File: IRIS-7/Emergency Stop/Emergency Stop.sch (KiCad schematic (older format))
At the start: 0 parts

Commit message: Setup the 12V buck converter
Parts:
- added C?: 100nF, symbol C_Small
- added C?: 2.2uF, symbol C
- added C?: 4.7uF, symbol C
- added D?: MBRS1100T3G, symbol D_Schottky
- added IC?: LMR16006X, symbol LMR16006X
- added JP1: JP_NC, symbol JP_NC
- added L?: 220uH, symbol L
- added P?: CONN_01X02, symbol CONN_01X02
- added P?: ESTOP, symbol SPST
- added R?: 88.7k, symbol R_Small
- added R?: 6.04k, symbol R_Small
- added R?: 620k, symbol R_Small
- added R?: 20k, symbol R_Small
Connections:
- net labels added: +12V, BOOT, FB, GND, SW
- wire segments 0 -> 36
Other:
- note added: "JP1—UVLO\nOpen: Disabled\nShort: Enabled"
- note added: "TODO:\n- Verify switch voltage rating"
- note added: "UVLO occurs at 40Vin"

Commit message: Add startup control to schematic
Schematic is now ready for layout
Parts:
- added C4: 4.7uF, symbol C
- added C5, C6: 1uF, Capacitors_SMD:C_0805, symbol C_Small
- added D2: Blue, LEDs:LED_0805, symbol Led_Small
- added D3: Green, LEDs:LED_0805, symbol Led_Small
- added D4: SMAJ40CA, Diodes_SMD:D_SMA_Standard, symbol TVS
- added J1: Pwr, Terminal_Blocks:TerminalBlock_Pheonix_MPT-2.54mm_4pol, symbol SPST-NOmC-LED
- added J2: Contactor, Terminal_Blocks:TerminalBlock_Pheonix_MKDS1.5-2pol, symbol CONN_01X02
- added JP2: JP_NO, Socket_Strips:Socket_Strip_Straight_1x02_Pitch2.54mm, symbol JP_NO
- added Q1, Q2: BSS123, TO_SOT_Packages_SMD:SOT-23, symbol BSS123
- added Q3: DMP3099L, TO_SOT_Packages_SMD:SOT-23, symbol DMP3099L
- added R10, R11, R5, R6, R7, R9: 10k, Resistors_SMD:R_0805, symbol R_Small
- added R8: 100k, Resistors_SMD:R_0805, symbol R_Small
- IC1: renamed from IC?; value LMR16006X -> LMR16006; symbol LMR16006X -> LMR16006
- JP1: footprint (none) -> Socket_Strips:Socket_Strip_Straight_1x02_Pitch2.54mm
- R1, R2, R3, R4: renamed from R?; footprint (none) -> Resistors_SMD:R_0805
- gave numbers to parts that had none: 7
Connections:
- net labels added: 12Vout, EN, ~EN
- wire segments 36 -> 69
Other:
- note added: "12V DC-DC Converter"
- note added: "Emergency Stop Control Logic"
- note added: "Enables IRIS-7 when the Estop is closed\nand the power button has been pressed"
- note added: "JP2—Startup Control\nOpen: Button press required\nShort: Immediate startup"
- note added: "Powers the main relay when the\nestop button is not pressed and\nthe input voltage is above 40V"
- note added: "τ = 100ms"
- note added: "τ = 10ms"
- moved on the sheet: C1, C2, C3, D1, JP1, L1, P1, P2, R1, R2, R3, R4

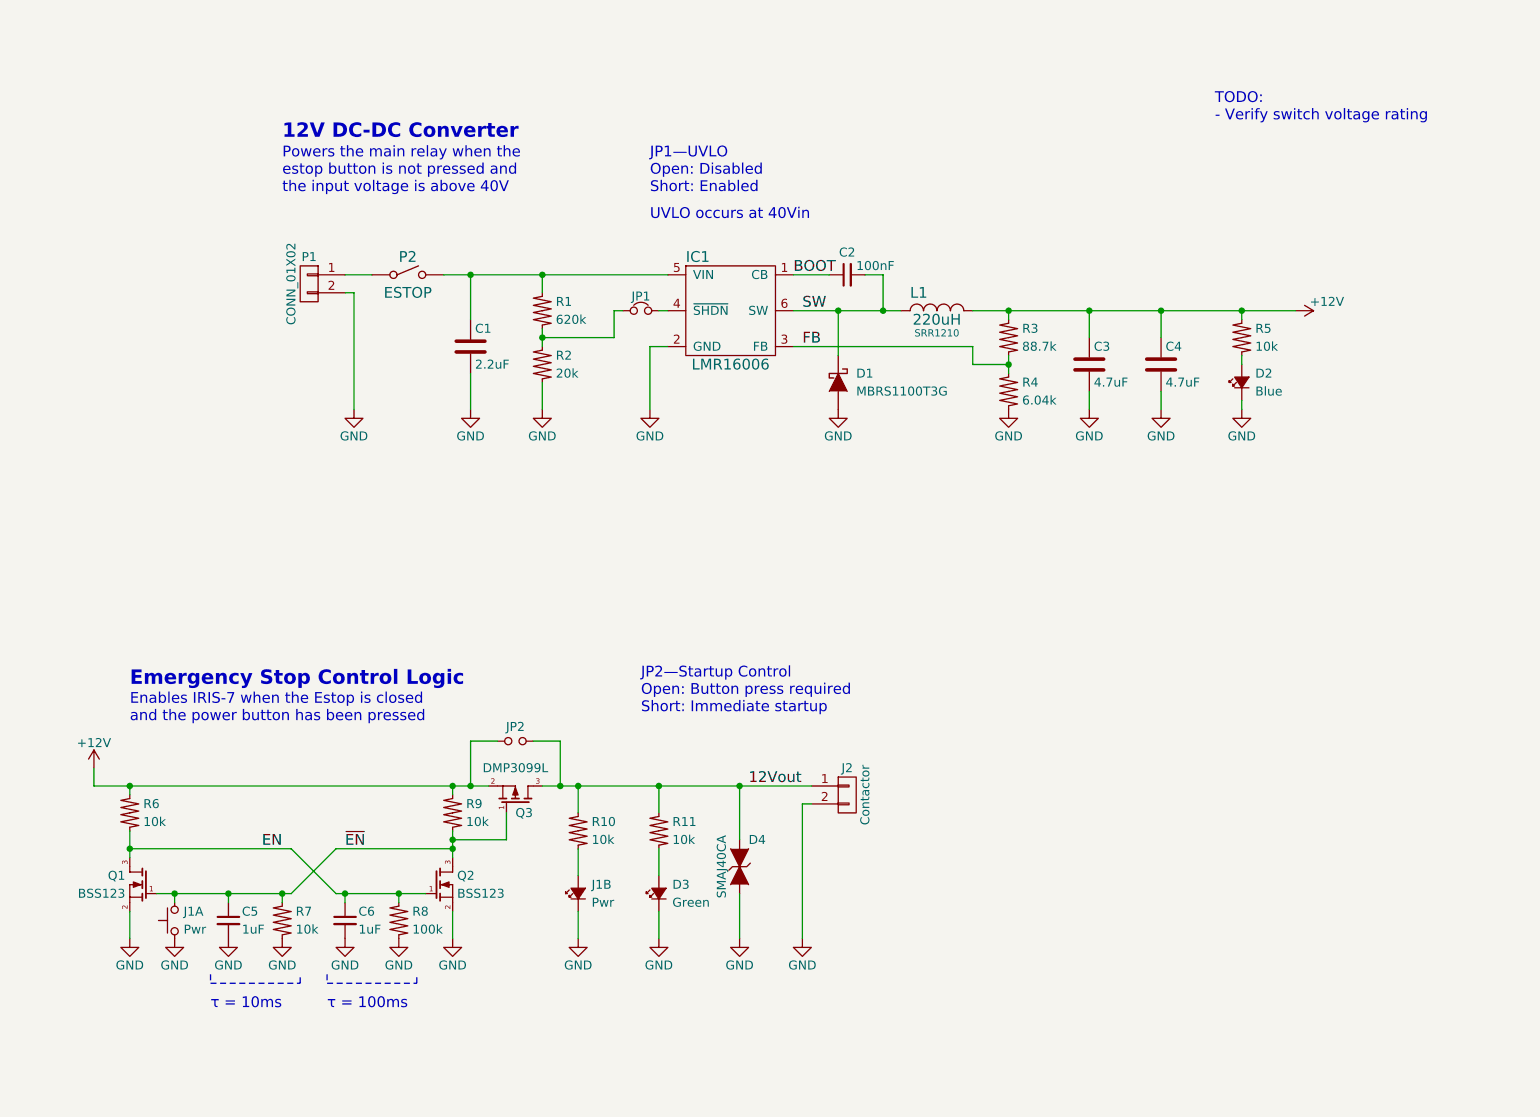
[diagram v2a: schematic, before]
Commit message: Complete component placement
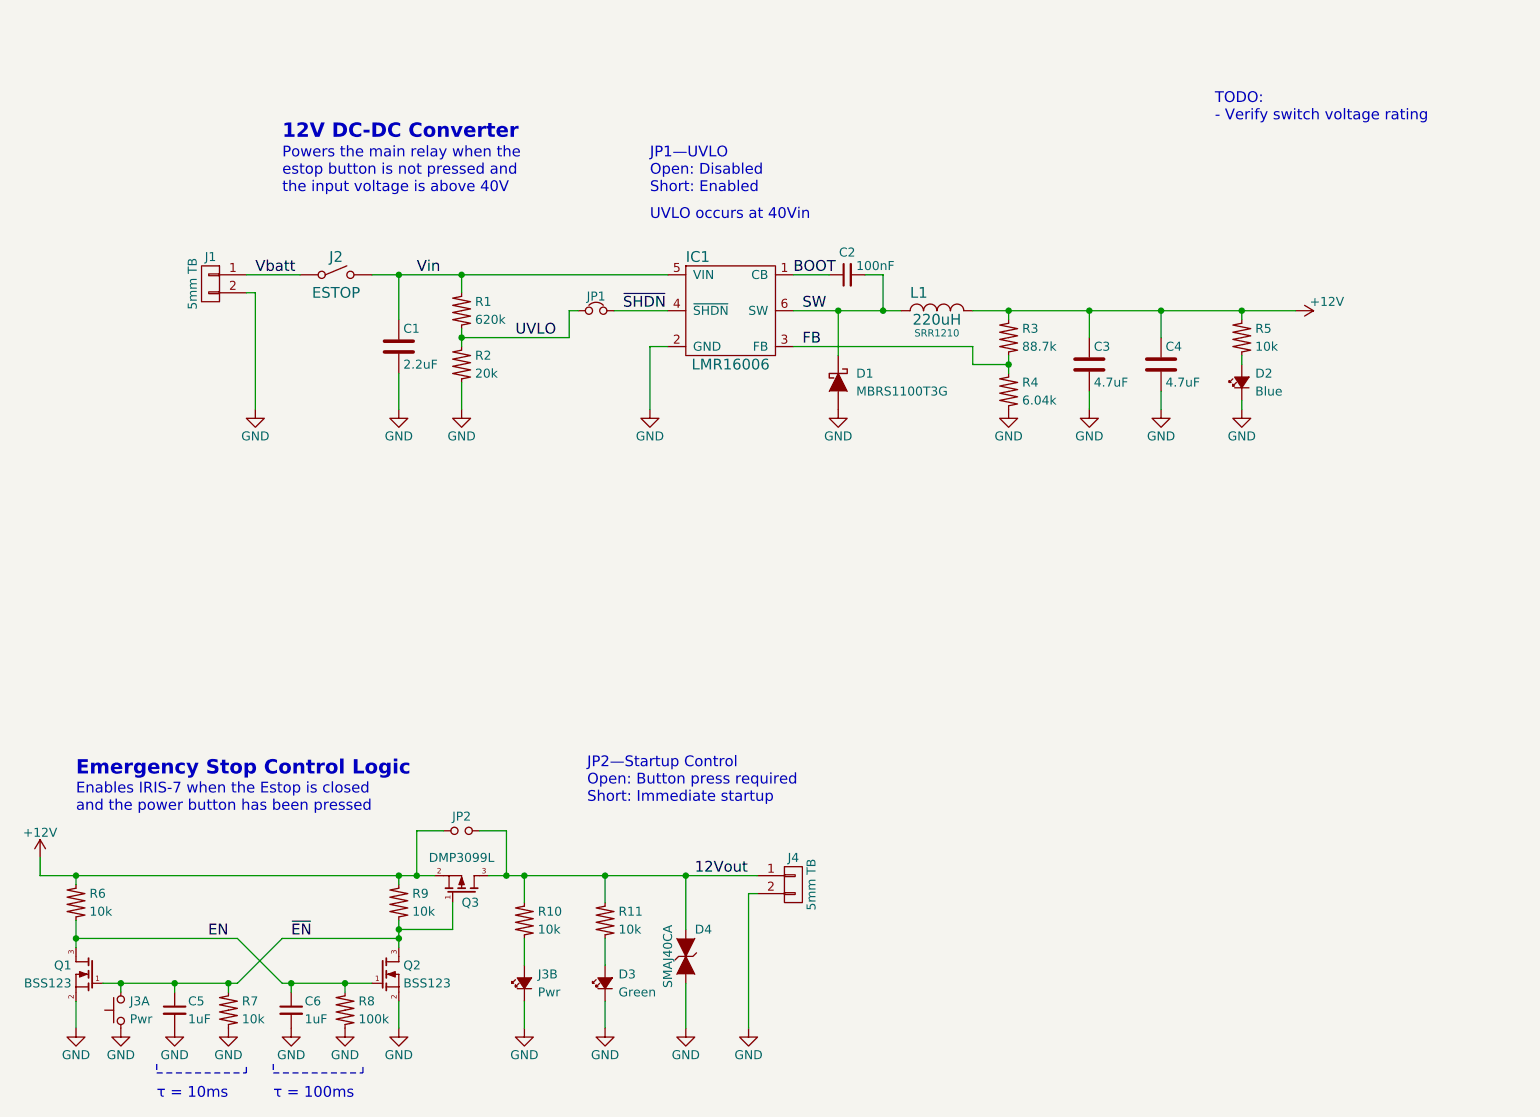
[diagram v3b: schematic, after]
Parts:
- C1, C2, C3, C4: footprint (none) -> Capacitors_SMD:C_0805
- D1: footprint (none) -> Diodes_SMD:D_SMB_Standard
- IC1: footprint (none) -> TO_SOT_Packages_SMD:TSOT-23-6_MK06A
- J1: renamed from P1; value CONN_01X02 -> 5mm TB; footprint (none) -> Terminal_Blocks:TerminalBlock_Pheonix_MKDS1.5-2pol
- J2: renamed from P2; footprint (none) -> Terminal_Blocks:TerminalBlock_Pheonix_MPT-2.54mm_2pol
- J4: renamed from J2; value Contactor -> 5mm TB
- L1: footprint (none) -> Choke_SMD:Choke_SMD_12x12mm_h8mm
- renumbered J1 to J3
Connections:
- net ~SHDN: now reaches IC1.4 (~SHDN), JP1.2
- net Vin: now reaches C1.1, IC1.5 (VIN), J2.2 (NO), R1.2
- net Vbatt: now reaches J1.1 (P1), J2.1 (COM)
- net UVLO: now reaches JP1.1, R1.1, R2.2
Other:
- moved on the sheet: C1, C5, C6, D3, D4, J1, J2, J3A, J3B, J4, JP1, JP2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

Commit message: Adjust wires in schematic
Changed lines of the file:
@@
 $EndComp
 Wire Wire Line
-	3150 2700 3300 2700
-Wire Wire Line
-	3300 2700 3650 2700
-Wire Wire Line
-	3650 2700 4800 2700
+	3150 2700 4800 2700
 Wire Wire Line
 	4800 3100 4700 3100
@@
 	5700 2700 5500 2700
 Wire Wire Line
-	5500 2900 5750 2900
-Wire Wire Line
-	5750 2900 6000 2900
-Wire Wire Line
-	6000 2900 6100 2900
+	5500 2900 6100 2900
 Wire Wire Line
 	5900 2700 6000 2700
@@
 $EndComp
 Wire Wire Line
-	6500 2900 6700 2900
-Wire Wire Line
-	6700 2900 7150 2900
-Wire Wire Line
-	7150 2900 7550 2900
-Wire Wire Line
-	7550 2900 8000 2900
-Wire Wire Line
-	8000 2900 8300 2900
+	6500 2900 8300 2900
 Wire Wire Line
 	6700 2900 6700 2950
 Connection ~ 6700 2900
 Wire Wire Line
-	6700 3150 6700 3200
-Wire Wire Line
-	6700 3200 6700 3250
+	6700 3150 6700 3250
 $Comp
 L GND #PWR03
@@
 	3650 3300 3650 3450
 Wire Wire Line
-	3650 3000 3650 3050
-Wire Wire Line
-	3650 3050 3650 3100
+	3650 3000 3650 3100
 Wire Wire Line
 	3650 2800 3650 2700
@@
 Enables IRIS-7 when the Estop is closed\nand the power button has been pressed
 Wire Wire Line
-	1500 6300 1500 6400
-Wire Wire Line
-	1500 6400 1500 6450
-Wire Wire Line
-	3300 6300 3300 6350
-Wire Wire Line
-	3300 6350 3300 6400
-Wire Wire Line
-	3300 6400 3300 6450
-Wire Wire Line
-	1650 6650 1750 6650
-Wire Wire Line
-	1750 6650 2050 6650
-Wire Wire Line
-	2050 6650 2350 6650
-Wire Wire Line
-	2350 6650 2400 6650
+	1500 6300 1500 6450
+Wire Wire Line
+	3300 6300 3300 6450
+Wire Wire Line
+	1650 6650 2400 6650
 Wire Wire Line
 	2400 6650 2650 6400
@@
 Connection ~ 3300 6400
 Wire Wire Line
-	2650 6650 2700 6650
-Wire Wire Line
-	2700 6650 3000 6650
-Wire Wire Line
-	3000 6650 3150 6650
+	2650 6650 3150 6650
 Wire Wire Line
 	2400 6400 2650 6650
@@
 Connection ~ 1500 6400
 Wire Wire Line
-	1300 6050 1500 6050
-Wire Wire Line
-	1500 6050 3300 6050
-Wire Wire Line
-	3300 6050 3400 6050
-Wire Wire Line
-	3400 6050 3500 6050
+	1300 6050 3500 6050
 Wire Wire Line
 	3300 6050 3300 6100
@@
 Connection ~ 3300 6350
 Wire Wire Line
-	3800 6050 3900 6050
-Wire Wire Line
-	3900 6050 4000 6050
-Wire Wire Line
-	4000 6050 4450 6050
-Wire Wire Line
-	4450 6050 4900 6050
-Wire Wire Line
-	4900 6050 5300 6050
+	3800 6050 5300 6050
 Wire Notes Line
 	1950 7100 1950 7150

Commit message: Finalize board design for Rev A release
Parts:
- added F1: 0.1A, Fuse_Holders_and_Fuses:Fuseholder5x20_horiz_open_Schurter_0031_8201, symbol F
- JP1, JP2: footprint Socket_Strips:Socket_Strip_Straight_1x02_Pitch2.54mm -> Pin_Headers:Pin_Header_Straight_1x02_Pitch2.54mm
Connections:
- net Vbatt: now also F1.1; no longer J2.1 (COM)
- new net Vestop: F1.2, J2.1 (COM)
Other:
- note added: "TODO:\n- Recalculate UVLO values"
- note removed: "TODO:\n- Verify switch voltage rating"
- moved on the sheet: J1
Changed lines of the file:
@@
 LIBS:Transistor
 LIBS:Estop_Lib
+LIBS:40xx Series
+LIBS:7400 Series
+LIBS:Connector
+LIBS:Generic Symbols
+LIBS:Linear Regulator
+LIBS:Linear Technology
+LIBS:LMxxx
+LIBS:microchip
+LIBS:ON Semiconductor
 LIBS:Emergency Stop-cache
 EELAYER 25 0
@@
 L CONN_01X02 J1
 U 1 1 58BE5E92
-P 2250 2750
-F 0 "J1" H 2250 2900 50  0000 C CNN
-F 1 "5mm TB" V 2350 2750 50  0000 C CNN
-F 2 "Terminal_Blocks:TerminalBlock_Pheonix_MKDS1.5-2pol" H 2250 2750 50  0001 C CNN
-F 3 "" H 2250 2750 50  0000 C CNN
-	1    2250 2750
+P 1450 2750
+F 0 "J1" H 1450 2900 50  0000 C CNN
+F 1 "5mm TB" V 1550 2750 50  0000 C CNN
+F 2 "Terminal_Blocks:TerminalBlock_Pheonix_MKDS1.5-2pol" H 1450 2750 50  0001 C CNN
+F 3 "" H 1450 2750 50  0000 C CNN
+	1    1450 2750
 	-1   0    0    -1
 $EndComp
@@
 $EndComp
 Wire Wire Line
-	2450 2800 2500 2800
-Wire Wire Line
-	2500 2800 2500 3450
-Wire Wire Line
-	2450 2700 2750 2700
-$Comp
-L GND #PWR01
+	1650 2800 1700 2800
+Wire Wire Line
+	1700 2800 1700 3450
+$Comp
+L GND #PWR3
 U 1 1 58BE5FF1
-P 2500 3450
-F 0 "#PWR01" H 2500 3200 50  0001 C CNN
-F 1 "GND" H 2500 3300 50  0000 C CNN
-F 2 "" H 2500 3450 50  0000 C CNN
-F 3 "" H 2500 3450 50  0000 C CNN
-	1    2500 3450
+P 1700 3450
+F 0 "#PWR3" H 1700 3200 50  0001 C CNN
+F 1 "GND" H 1700 3300 50  0000 C CNN
+F 2 "" H 1700 3450 50  0000 C CNN
+F 3 "" H 1700 3450 50  0000 C CNN
+	1    1700 3450
 	1    0    0    -1
 $EndComp
@@
 	4700 3100 4700 3450
 $Comp
-L GND #PWR02
+L GND #PWR14
 U 1 1 58BE6084
 P 4700 3450
-F 0 "#PWR02" H 4700 3200 50  0001 C CNN
+F 0 "#PWR14" H 4700 3200 50  0001 C CNN
 F 1 "GND" H 4700 3300 50  0000 C CNN
 F 2 "" H 4700 3450 50  0000 C CNN
@@
 	6700 3150 6700 3250
 $Comp
-L GND #PWR03
+L GND #PWR18
 U 1 1 58BE679C
 P 6700 3450
-F 0 "#PWR03" H 6700 3200 50  0001 C CNN
+F 0 "#PWR18" H 6700 3200 50  0001 C CNN
 F 1 "GND" H 6700 3300 50  0000 C CNN
 F 2 "" H 6700 3450 50  0000 C CNN
@@
 Connection ~ 6700 3200
 $Comp
-L GND #PWR04
+L GND #PWR17
 U 1 1 58BE6802
 P 5750 3450
-F 0 "#PWR04" H 5750 3200 50  0001 C CNN
+F 0 "#PWR17" H 5750 3200 50  0001 C CNN
 F 1 "GND" H 5750 3300 50  0000 C CNN
 F 2 "" H 5750 3450 50  0000 C CNN
@@
 Connection ~ 5750 2900
 Text Notes 7850 1850 0    60   ~ 0
-TODO:\n- Verify switch voltage rating
+TODO:\n- Recalculate UVLO values
 $Comp
 L C C1
@@
 $EndComp
 $Comp
-L GND #PWR05
+L GND #PWR9
 U 1 1 58BE6EAE
 P 3300 3450
-F 0 "#PWR05" H 3300 3200 50  0001 C CNN
+F 0 "#PWR9" H 3300 3200 50  0001 C CNN
 F 1 "GND" H 3300 3300 50  0000 C CNN
 F 2 "" H 3300 3450 50  0000 C CNN
@@
 	7150 3350 7150 3450
 $Comp
-L GND #PWR06
+L GND #PWR19
 U 1 1 58BE718D
 P 7150 3450
-F 0 "#PWR06" H 7150 3200 50  0001 C CNN
+F 0 "#PWR19" H 7150 3200 50  0001 C CNN
 F 1 "GND" H 7150 3300 50  0000 C CNN
 F 2 "" H 7150 3450 50  0000 C CNN
@@
 $EndComp
 $Comp
-L +12V #PWR07
+L +12V #PWR22
 U 1 1 58BE7361
 P 8300 2900
-F 0 "#PWR07" H 8300 2750 50  0001 C CNN
+F 0 "#PWR22" H 8300 2750 50  0001 C CNN
 F 1 "+12V" V 8250 3075 50  0000 C CNN
 F 2 "" H 8300 2900 50  0000 C CNN
@@
 $EndComp
 $Comp
-L GND #PWR08
+L GND #PWR11
 U 1 1 58BE68B7
 P 3650 3450
-F 0 "#PWR08" H 3650 3200 50  0001 C CNN
+F 0 "#PWR11" H 3650 3200 50  0001 C CNN
 F 1 "GND" H 3650 3300 50  0000 C CNN
 F 2 "" H 3650 3450 50  0000 C CNN
@@
 F 0 "JP1" H 4400 2980 50  0000 C CNN
 F 1 "JP_NC" H 4410 2840 50  0001 C CNN
-F 2 "Socket_Strips:Socket_Strip_Straight_1x02_Pitch2.54mm" H 4400 2900 50  0001 C CNN
+F 2 "Pin_Headers:Pin_Header_Straight_1x02_Pitch2.54mm" H 4400 2900 50  0001 C CNN
 F 3 "" H 4400 2900 50  0000 C CNN
 	1    4400 2900
@@
 $EndComp
 $Comp
-L GND #PWR09
+L GND #PWR7
 U 1 1 58BF8662
 P 2700 6900
-F 0 "#PWR09" H 2700 6650 50  0001 C CNN
+F 0 "#PWR7" H 2700 6650 50  0001 C CNN
 F 1 "GND" H 2700 6750 50  0000 C CNN
 F 2 "" H 2700 6900 50  0000 C CNN
@@
 $EndComp
 $Comp
-L GND #PWR010
+L GND #PWR8
 U 1 1 58BF8668
 P 3000 6900
-F 0 "#PWR010" H 3000 6650 50  0001 C CNN
+F 0 "#PWR8" H 3000 6650 50  0001 C CNN
 F 1 "GND" H 3000 6750 50  0000 C CNN
 F 2 "" H 3000 6900 50  0000 C CNN
@@
 $EndComp
 $Comp
-L GND #PWR011
+L GND #PWR10
 U 1 1 58BF866E
 P 3300 6900
-F 0 "#PWR011" H 3300 6650 50  0001 C CNN
+F 0 "#PWR10" H 3300 6650 50  0001 C CNN
 F 1 "GND" H 3300 6750 50  0000 C CNN
 F 2 "" H 3300 6900 50  0000 C CNN
@@
 $EndComp
 $Comp
-L GND #PWR012
+L GND #PWR6
 U 1 1 58BF8674
 P 2350 6900
-F 0 "#PWR012" H 2350 6650 50  0001 C CNN
+F 0 "#PWR6" H 2350 6650 50  0001 C CNN
 F 1 "GND" H 2350 6750 50  0000 C CNN
 F 2 "" H 2350 6900 50  0000 C CNN
@@
 $EndComp
 $Comp
-L GND #PWR013
+L GND #PWR5
 U 1 1 58BF867A
 P 2050 6900
-F 0 "#PWR013" H 2050 6650 50  0001 C CNN
+F 0 "#PWR5" H 2050 6650 50  0001 C CNN
 F 1 "GND" H 2050 6750 50  0000 C CNN
 F 2 "" H 2050 6900 50  0000 C CNN
@@
 $EndComp
 $Comp
-L GND #PWR014
+L GND #PWR4
 U 1 1 58BF8680
 P 1750 6900
-F 0 "#PWR014" H 1750 6650 50  0001 C CNN
+F 0 "#PWR4" H 1750 6650 50  0001 C CNN
 F 1 "GND" H 1750 6750 50  0000 C CNN
 F 2 "" H 1750 6900 50  0000 C CNN
@@
 $EndComp
 $Comp
-L GND #PWR015
+L GND #PWR2
 U 1 1 58BF8686
 P 1500 6900
-F 0 "#PWR015" H 1500 6650 50  0001 C CNN
+F 0 "#PWR2" H 1500 6650 50  0001 C CNN
 F 1 "GND" H 1500 6750 50  0000 C CNN
 F 2 "" H 1500 6900 50  0000 C CNN
@@
 $EndComp
 $Comp
-L GND #PWR016
+L GND #PWR16
 U 1 1 58BF8697
 P 5250 6900
-F 0 "#PWR016" H 5250 6650 50  0001 C CNN
+F 0 "#PWR16" H 5250 6650 50  0001 C CNN
 F 1 "GND" H 5250 6750 50  0000 C CNN
 F 2 "" H 5250 6900 50  0000 C CNN
@@
 $EndComp
 $Comp
-L +12V #PWR017
+L +12V #PWR1
 U 1 1 58BF869E
 P 1300 5950
-F 0 "#PWR017" H 1300 5800 50  0001 C CNN
+F 0 "#PWR1" H 1300 5800 50  0001 C CNN
 F 1 "+12V" H 1300 6090 50  0000 C CNN
 F 2 "" H 1300 5950 50  0000 C CNN
@@
 $EndComp
 $Comp
-L GND #PWR018
+L GND #PWR12
 U 1 1 58BF86CF
 P 4000 6900
-F 0 "#PWR018" H 4000 6650 50  0001 C CNN
+F 0 "#PWR12" H 4000 6650 50  0001 C CNN
 F 1 "GND" H 4000 6750 50  0000 C CNN
 F 2 "" H 4000 6900 50  0000 C CNN
@@
 $EndComp
 $Comp
-L GND #PWR019
+L GND #PWR15
 U 1 1 58BF86DC
 P 4900 6900
-F 0 "#PWR019" H 4900 6650 50  0001 C CNN
+F 0 "#PWR15" H 4900 6650 50  0001 C CNN
 F 1 "GND" H 4900 6750 50  0000 C CNN
 F 2 "" H 4900 6900 50  0000 C CNN
@@
 $EndComp
 $Comp
-L GND #PWR020
+L GND #PWR21
 U 1 1 58BFEC22
 P 8000 3450
-F 0 "#PWR020" H 8000 3200 50  0001 C CNN
+F 0 "#PWR21" H 8000 3200 50  0001 C CNN
 F 1 "GND" H 8000 3300 50  0000 C CNN
 F 2 "" H 8000 3450 50  0000 C CNN
@@
 $EndComp
 $Comp
-L GND #PWR021
+L GND #PWR13
 U 1 1 58BFFF1E
 P 4450 6900
-F 0 "#PWR021" H 4450 6650 50  0001 C CNN
+F 0 "#PWR13" H 4450 6650 50  0001 C CNN
 F 1 "GND" H 4450 6750 50  0000 C CNN
 F 2 "" H 4450 6900 50  0000 C CNN
@@
 F 0 "JP2" H 3650 5880 50  0000 C CNN
 F 1 "JP_NO" H 3660 5740 50  0001 C CNN
-F 2 "Socket_Strips:Socket_Strip_Straight_1x02_Pitch2.54mm" H 3650 5800 50  0001 C CNN
+F 2 "Pin_Headers:Pin_Header_Straight_1x02_Pitch2.54mm" H 3650 5800 50  0001 C CNN
 F 3 "" H 3650 5800 50  0000 C CNN
 	1    3650 5800
@@
 	7550 3350 7550 3450
 $Comp
-L GND #PWR022
+L GND #PWR20
 U 1 1 58C0735E
 P 7550 3450
-F 0 "#PWR022" H 7550 3200 50  0001 C CNN
+F 0 "#PWR20" H 7550 3200 50  0001 C CNN
 F 1 "GND" H 7550 3300 50  0000 C CNN
 F 2 "" H 7550 3450 50  0000 C CNN
@@
 Wire Wire Line
 	4250 2900 4300 2900
-Text Label 2500 2700 0    60   ~ 0
-Vbatt
 Text Label 3400 2700 0    60   ~ 0
 Vin
+$Comp
+L F F1
+U 1 1 58FE6CC4
+P 2100 2700
+F 0 "F1" H 2000 2750 60  0000 C CNN
+F 1 "0.1A" H 2150 2650 60  0000 L CNN
+F 2 "Fuse_Holders_and_Fuses:Fuseholder5x20_horiz_open_Schurter_0031_8201" H 2100 2700 60  0001 C CNN
+F 3 "" H 2100 2700 60  0000 C CNN
+	1    2100 2700
+	1    0    0    -1
+$EndComp
+Wire Wire Line
+	1650 2700 1900 2700
+Wire Wire Line
+	2300 2700 2750 2700
+Text Label 1650 2700 0    60   ~ 0
+Vbatt
+Text Label 2400 2700 0    60   ~ 0
+Vestop
 $EndSCHEMATC
